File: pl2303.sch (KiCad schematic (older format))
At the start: 26 parts, among them P2 USB_OTG, U2 PL2303, Y1 CRYSTAL

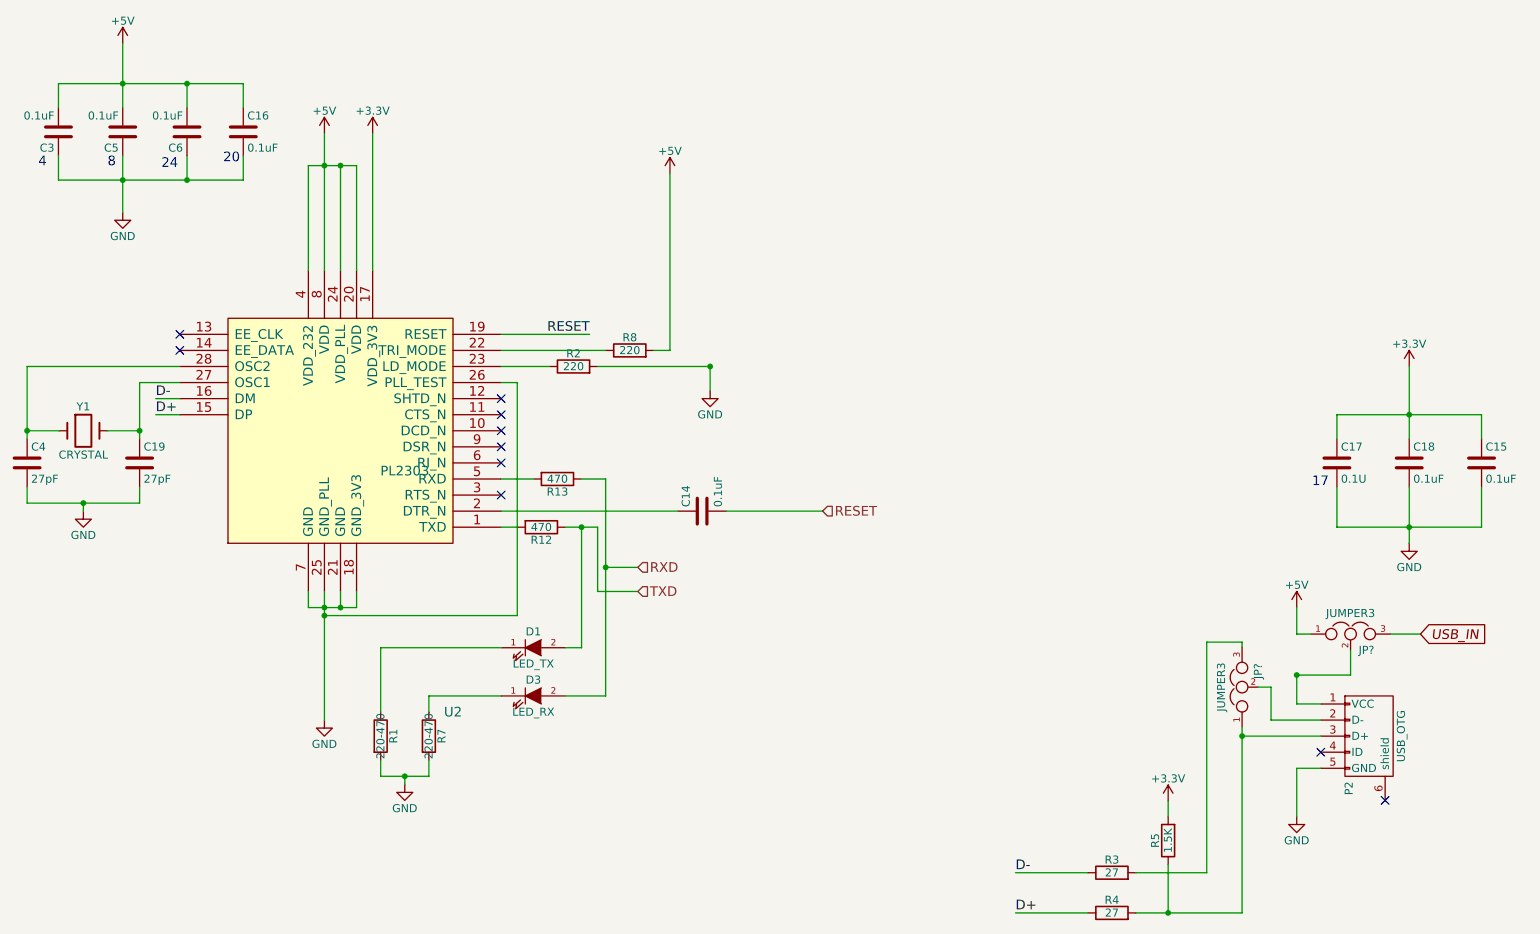
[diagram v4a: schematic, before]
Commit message: разделение питания и добавление потенциометра у лмки
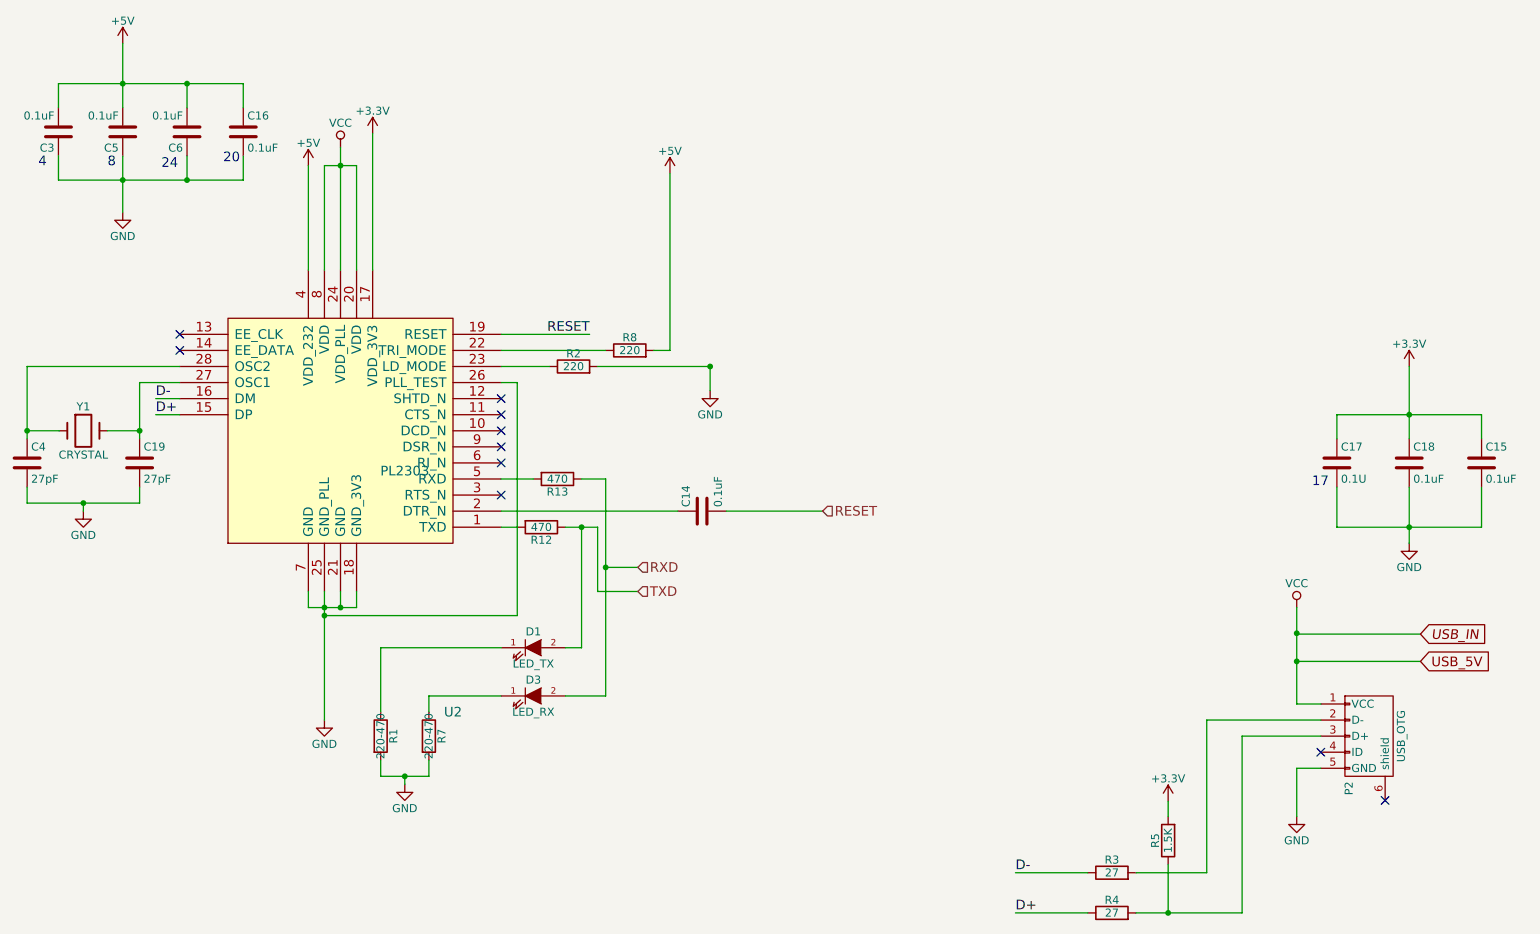
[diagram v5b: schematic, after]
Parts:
- removed JP? (x2): JUMPER3, symbol JUMPER3
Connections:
- net +5V: no longer U2.20 (VDD), U2.24 (VDD_PLL), U2.8 (VDD)
- net at R3.2: now also P2.2 (D-)
- net VCC: now reaches P2.1 (VCC)
- net VCC: now also U2.20 (VDD), U2.24 (VDD_PLL), U2.8 (VDD)
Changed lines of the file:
@@
 L +5V #PWR031
 U 1 1 5717F490
-P 2450 1450
-F 0 "#PWR031" H 2450 1300 50  0001 C CNN
-F 1 "+5V" H 2450 1590 50  0000 C CNN
-F 2 "" H 2450 1450 50  0000 C CNN
-F 3 "" H 2450 1450 50  0000 C CNN
-	1    2450 1450
+P 2350 1650
+F 0 "#PWR031" H 2350 1500 50  0001 C CNN
+F 1 "+5V" H 2350 1790 50  0000 C CNN
+F 2 "" H 2350 1650 50  0000 C CNN
+F 3 "" H 2350 1650 50  0000 C CNN
+	1    2350 1650
 	1    0    0    -1
 $EndComp
@@
 Connection ~ 4850 2900
 Wire Wire Line
-	2550 1650 2550 2300
+	2550 1535 2550 2300
 Wire Wire Line
 	795  1590 795  1740
@@
 	2350 2300 2350 1650
 Wire Wire Line
-	2350 1650 2650 1650
+	2450 1650 2650 1650
 Wire Wire Line
 	4850 2900 4850 3050
 Wire Wire Line
-	2450 1450 2450 2300
-Connection ~ 2450 1650
+	2450 1650 2450 2300
 Wire Wire Line
 	2550 4400 2550 4300
@@
 Connection ~ 2550 4400
 Wire Wire Line
-	8650 5000 8500 5000
-$Comp
-L +5V #PWR032
-U 1 1 571E81DD
-P 8500 4400
-F 0 "#PWR032" H 8500 4250 50  0001 C CNN
-F 1 "+5V" H 8500 4540 50  0000 C CNN
-F 2 "" H 8500 4400 50  0000 C CNN
-F 3 "" H 8500 4400 50  0000 C CNN
-	1    8500 4400
-	1    0    0    -1
-$EndComp
+	8500 5000 8650 5000
 $Comp
 L +5V #PWR033
@@
 	7940 6050 7500 6050
 Wire Wire Line
-	8160 5145 8160 6300
-Wire Wire Line
-	8160 6300 7500 6300
-Wire Wire Line
-	7940 4615 7940 6050
-$Comp
-L JUMPER3 JP?
-U 1 1 577BDA08
-P 8160 4895
-F 0 "JP?" H 8210 4795 50  0000 L CNN
-F 1 "JUMPER3" H 8160 4995 50  0000 C BNN
-F 2 "" H 8160 4895 50  0000 C CNN
-F 3 "" H 8160 4895 50  0000 C CNN
-	1    8160 4895
-	0    -1   -1   0
-$EndComp
-Wire Wire Line
-	8650 5100 8340 5100
-Wire Wire Line
-	8340 5100 8340 4895
-Wire Wire Line
-	8340 4895 8260 4895
-Connection ~ 8160 5200
-Wire Wire Line
-	8160 4645 8160 4615
-Wire Wire Line
-	8160 4615 7940 4615
-$Comp
-L JUMPER3 JP?
-U 1 1 577BEAFF
-P 8835 4565
-F 0 "JP?" H 8885 4465 50  0000 L CNN
-F 1 "JUMPER3" H 8835 4665 50  0000 C BNN
-F 2 "" H 8835 4565 50  0000 C CNN
-F 3 "" H 8835 4565 50  0000 C CNN
-	1    8835 4565
-	1    0    0    -1
-$EndComp
-Wire Wire Line
-	8500 4820 8835 4820
-Wire Wire Line
-	8835 4820 8835 4665
-Connection ~ 8500 4820
-Wire Wire Line
-	8500 5000 8500 4820
-Wire Wire Line
-	8585 4565 8500 4565
-Wire Wire Line
-	8500 4565 8500 4400
-Wire Wire Line
-	9085 4565 9270 4565
+	8160 6300 8160 5200
+Wire Wire Line
+	7500 6300 8160 6300
+Wire Wire Line
+	8500 4400 8500 5000
+Wire Wire Line
+	8500 4565 9270 4565
 Text GLabel 9270 4565 2    60   Input Italic 0
 USB_IN
+$Comp
+L VCC #PWR?
+U 1 1 578E438E
+P 8500 4400
+F 0 "#PWR?" H 8500 4250 50  0001 C CNN
+F 1 "VCC" H 8500 4550 50  0000 C CNN
+F 2 "" H 8500 4400 50  0000 C CNN
+F 3 "" H 8500 4400 50  0000 C CNN
+	1    8500 4400
+	1    0    0    -1
+$EndComp
+Wire Wire Line
+	8650 5100 7940 5100
+Wire Wire Line
+	7940 5100 7940 6050
+$Comp
+L VCC #PWR?
+U 1 1 578E507F
+P 2550 1535
+F 0 "#PWR?" H 2550 1385 50  0001 C CNN
+F 1 "VCC" H 2550 1685 50  0000 C CNN
+F 2 "" H 2550 1535 50  0000 C CNN
+F 3 "" H 2550 1535 50  0000 C CNN
+	1    2550 1535
+	1    0    0    -1
+$EndComp
+Wire Wire Line
+	8500 4565 8500 4560
+Connection ~ 8500 4560
+Wire Wire Line
+	8500 4735 9270 4735
+Connection ~ 8500 4735
+Text GLabel 9270 4735 2    60   Input ~ 0
+USB_5V
 $EndSCHEMATC

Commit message: Добавлен AMS1117 и изменения в питании
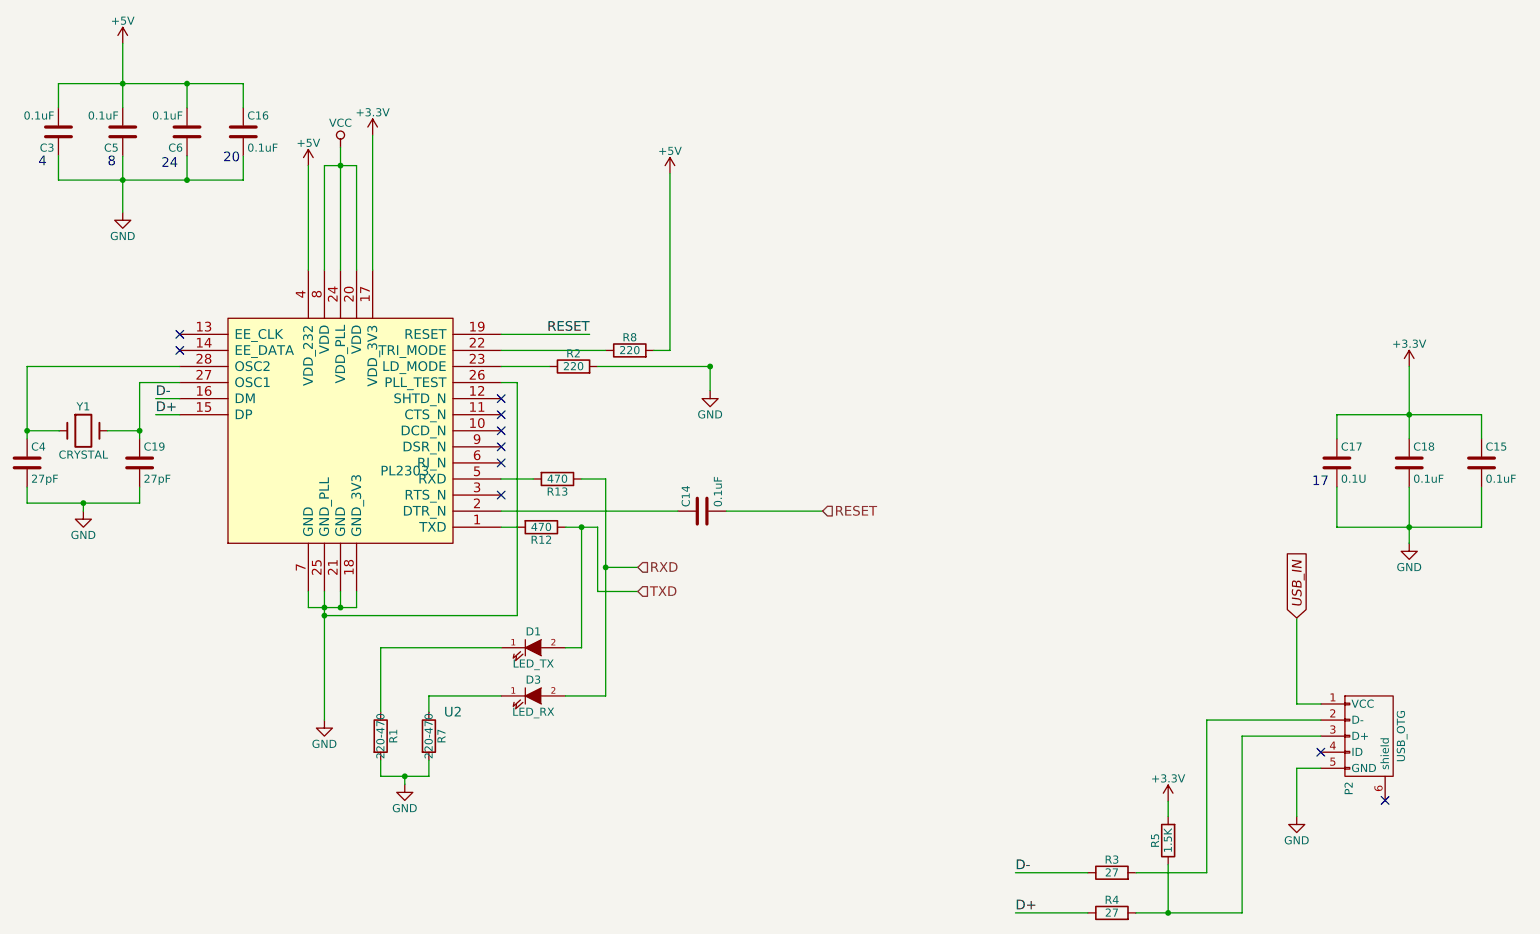
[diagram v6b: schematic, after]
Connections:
- net VCC: no longer P2.1 (VCC)
- new net USB_IN: P2.1 (VCC)
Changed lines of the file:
@@
 $EndComp
 $Comp
-L GND #PWR022
+L GND #PWR027
 U 1 1 5705278D
 P 9200 4000
-F 0 "#PWR022" H 9200 3750 50  0001 C CNN
+F 0 "#PWR027" H 9200 3750 50  0001 C CNN
 F 1 "GND" H 9200 3850 50  0000 C CNN
 F 2 "" H 9200 4000 50  0000 C CNN
@@
 $EndComp
 $Comp
-L GND #PWR023
+L GND #PWR028
 U 1 1 570529E3
 P 8500 5700
-F 0 "#PWR023" H 8500 5450 50  0001 C CNN
+F 0 "#PWR028" H 8500 5450 50  0001 C CNN
 F 1 "GND" H 8500 5550 50  0000 C CNN
 F 2 "" H 8500 5700 50  0000 C CNN
@@
 $EndComp
 $Comp
-L GND #PWR024
+L GND #PWR029
 U 1 1 570620C0
 P 2950 5500
-F 0 "#PWR024" H 2950 5250 50  0001 C CNN
+F 0 "#PWR029" H 2950 5250 50  0001 C CNN
 F 1 "GND" H 2950 5350 50  0000 C CNN
 F 2 "" H 2950 5500 50  0000 C CNN
@@
 $EndComp
 $Comp
-L GND #PWR025
+L GND #PWR030
 U 1 1 570D14D2
 P 950 3800
-F 0 "#PWR025" H 950 3550 50  0001 C CNN
+F 0 "#PWR030" H 950 3550 50  0001 C CNN
 F 1 "GND" H 950 3650 50  0000 C CNN
 F 2 "" H 950 3800 50  0000 C CNN
@@
 NoConn ~ 3550 3700
 $Comp
-L GND #PWR026
+L GND #PWR031
 U 1 1 570D2EBB
 P 2450 5100
-F 0 "#PWR026" H 2450 4850 50  0001 C CNN
+F 0 "#PWR031" H 2450 4850 50  0001 C CNN
 F 1 "GND" H 2450 4950 50  0000 C CNN
 F 2 "" H 2450 5100 50  0000 C CNN
@@
 $EndComp
 $Comp
-L GND #PWR027
+L GND #PWR032
 U 1 1 570D2F71
 P 4850 3050
-F 0 "#PWR027" H 4850 2800 50  0001 C CNN
+F 0 "#PWR032" H 4850 2800 50  0001 C CNN
 F 1 "GND" H 4850 2900 50  0000 C CNN
 F 2 "" H 4850 3050 50  0000 C CNN
@@
 $EndComp
 $Comp
-L +3.3V #PWR028
+L +3.3V #PWR033
 U 1 1 570D3933
 P 9200 2900
-F 0 "#PWR028" H 9200 2750 50  0001 C CNN
+F 0 "#PWR033" H 9200 2750 50  0001 C CNN
 F 1 "+3.3V" H 9200 3040 50  0000 C CNN
 F 2 "" H 9200 2900 50  0000 C CNN
@@
 $EndComp
 $Comp
-L +5V #PWR029
+L +5V #PWR034
 U 1 1 5717E4F4
 P 1195 890
-F 0 "#PWR029" H 1195 740 50  0001 C CNN
+F 0 "#PWR034" H 1195 740 50  0001 C CNN
 F 1 "+5V" H 1195 1030 50  0000 C CNN
 F 2 "" H 1195 890 50  0000 C CNN
@@
 $EndComp
 $Comp
-L GND #PWR030
+L GND #PWR035
 U 1 1 5717E503
 P 1195 1940
-F 0 "#PWR030" H 1195 1690 50  0001 C CNN
+F 0 "#PWR035" H 1195 1690 50  0001 C CNN
 F 1 "GND" H 1195 1790 50  0000 C CNN
 F 2 "" H 1195 1940 50  0000 C CNN
@@
 $EndComp
 $Comp
-L +5V #PWR031
+L +5V #PWR036
 U 1 1 5717F490
 P 2350 1650
-F 0 "#PWR031" H 2350 1500 50  0001 C CNN
+F 0 "#PWR036" H 2350 1500 50  0001 C CNN
 F 1 "+5V" H 2350 1790 50  0000 C CNN
 F 2 "" H 2350 1650 50  0000 C CNN
@@
 Wire Wire Line
 	4150 4300 4400 4300
-Wire Wire Line
-	2750 1450 2750 2300
 $Comp
 L C C15
@@
 	8500 5000 8650 5000
 $Comp
-L +5V #PWR033
+L +5V #PWR037
 U 1 1 571E851C
 P 4600 1700
-F 0 "#PWR033" H 4600 1550 50  0001 C CNN
+F 0 "#PWR037" H 4600 1550 50  0001 C CNN
 F 1 "+5V" H 4600 1840 50  0000 C CNN
 F 2 "" H 4600 1700 50  0000 C CNN
@@
 	7700 5700 7700 5605
 $Comp
-L +3.3V #PWR034
+L +3.3V #PWR038
 U 1 1 574DBF4C
 P 7700 5605
-F 0 "#PWR034" H 7700 5455 50  0001 C CNN
+F 0 "#PWR038" H 7700 5455 50  0001 C CNN
 F 1 "+3.3V" H 7700 5745 50  0000 C CNN
 F 2 "" H 7700 5605 50  0000 C CNN
@@
 $EndComp
 $Comp
-L +3.3V #PWR035
+L +3.3V #PWR039
 U 1 1 574DC8B0
-P 2750 1450
-F 0 "#PWR035" H 2750 1300 50  0001 C CNN
-F 1 "+3.3V" H 2750 1590 50  0000 C CNN
-F 2 "" H 2750 1450 50  0000 C CNN
-F 3 "" H 2750 1450 50  0000 C CNN
-	1    2750 1450
+P 2750 1460
+F 0 "#PWR039" H 2750 1310 50  0001 C CNN
+F 1 "+3.3V" H 2750 1600 50  0000 C CNN
+F 2 "" H 2750 1460 50  0000 C CNN
+F 3 "" H 2750 1460 50  0000 C CNN
+	1    2750 1460
 	1    0    0    -1
 $EndComp
@@
 Wire Wire Line
 	7500 6300 8160 6300
-Wire Wire Line
-	8500 4400 8500 5000
-Wire Wire Line
-	8500 4565 9270 4565
-Text GLabel 9270 4565 2    60   Input Italic 0
+Text GLabel 8500 4465 1    60   Input Italic 0
 USB_IN
-$Comp
-L VCC #PWR?
-U 1 1 578E438E
-P 8500 4400
-F 0 "#PWR?" H 8500 4250 50  0001 C CNN
-F 1 "VCC" H 8500 4550 50  0000 C CNN
-F 2 "" H 8500 4400 50  0000 C CNN
-F 3 "" H 8500 4400 50  0000 C CNN
-	1    8500 4400
-	1    0    0    -1
-$EndComp
 Wire Wire Line
 	8650 5100 7940 5100
@@
 	7940 5100 7940 6050
 $Comp
-L VCC #PWR?
+L VCC #PWR040
 U 1 1 578E507F
 P 2550 1535
-F 0 "#PWR?" H 2550 1385 50  0001 C CNN
+F 0 "#PWR040" H 2550 1385 50  0001 C CNN
 F 1 "VCC" H 2550 1685 50  0000 C CNN
 F 2 "" H 2550 1535 50  0000 C CNN
@@
 $EndComp
 Wire Wire Line
-	8500 4565 8500 4560
-Connection ~ 8500 4560
-Wire Wire Line
-	8500 4735 9270 4735
-Connection ~ 8500 4735
-Text GLabel 9270 4735 2    60   Input ~ 0
-USB_5V
+	8500 5000 8500 4465
+Wire Wire Line
+	2750 1460 2750 2300
 $EndSCHEMATC
